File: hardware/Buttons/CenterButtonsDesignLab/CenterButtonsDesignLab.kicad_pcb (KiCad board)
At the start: 2 copper layers, 28 x 99 mm, 6 parts, among them J1 Conn_01x01, J2 Conn_01x01, J3 Conn_01x03, SW1 SW_Push, SW2 SW_Push, SW3 SW_Push

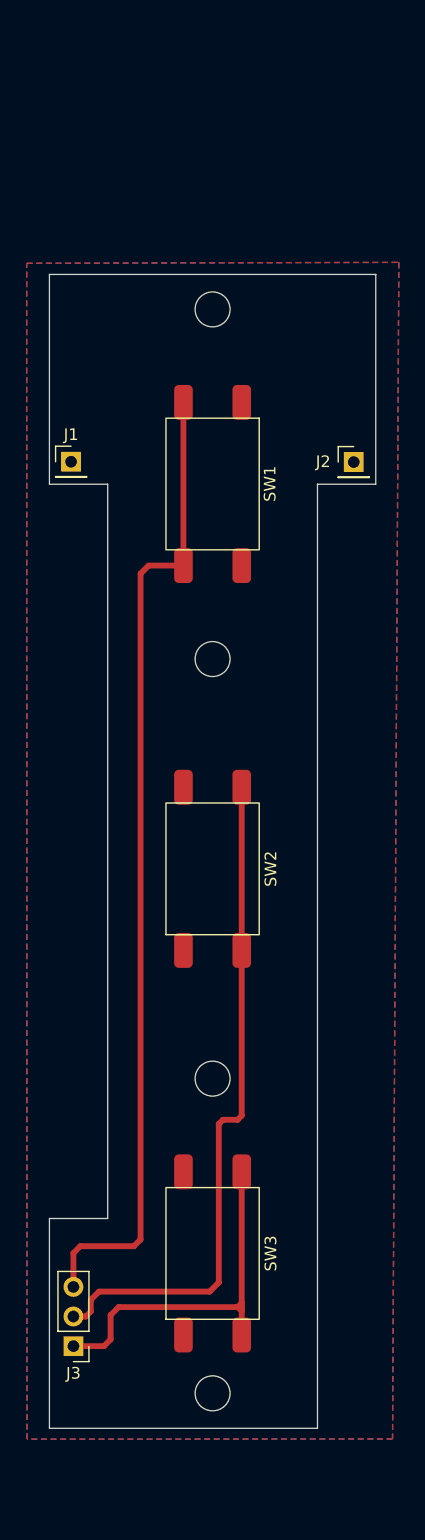
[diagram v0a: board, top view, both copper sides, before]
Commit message: Changes of button started
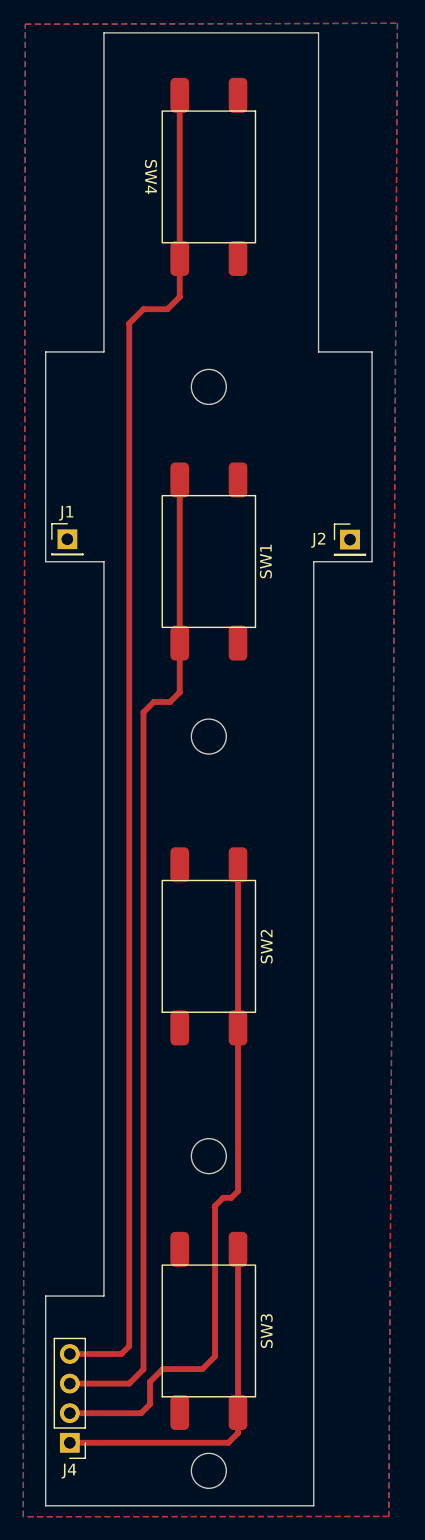
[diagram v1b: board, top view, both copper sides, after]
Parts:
- removed J3: Conn_01x03, Connector_PinHeader_2.54mm:PinHeader_1x03_P2.54mm_Vertical
- added J4: Conn_01x04, Connector_PinHeader_2.54mm:PinHeader_1x04_P2.54mm_Vertical, F.Cu at (166.9, 140.3)
- added SW4: SW_Push, Design:Button, F.Cu at (178.8, 31.7)
- moved J1 6.66 mm to (166.7, 62.7)
- moved SW3 6.66 mm to (178.8, 130.7)
- moved J2 6.66 mm to (190.9, 62.8)
- moved SW1 6.66 mm to (178.8, 64.7)
- moved SW2 6.66 mm to (178.8, 97.7)
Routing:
- net /D9: track 0.00 -> 115.7 mm
- net /D7: track 32.2 -> 30.5 mm
- net /D1: track 84.2 -> 85.2 mm
- net /D4: track 58.3 -> 59.0 mm
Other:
- board size 28 x 99 mm -> 28 x 126.4 mm

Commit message: New changes in the center buttons
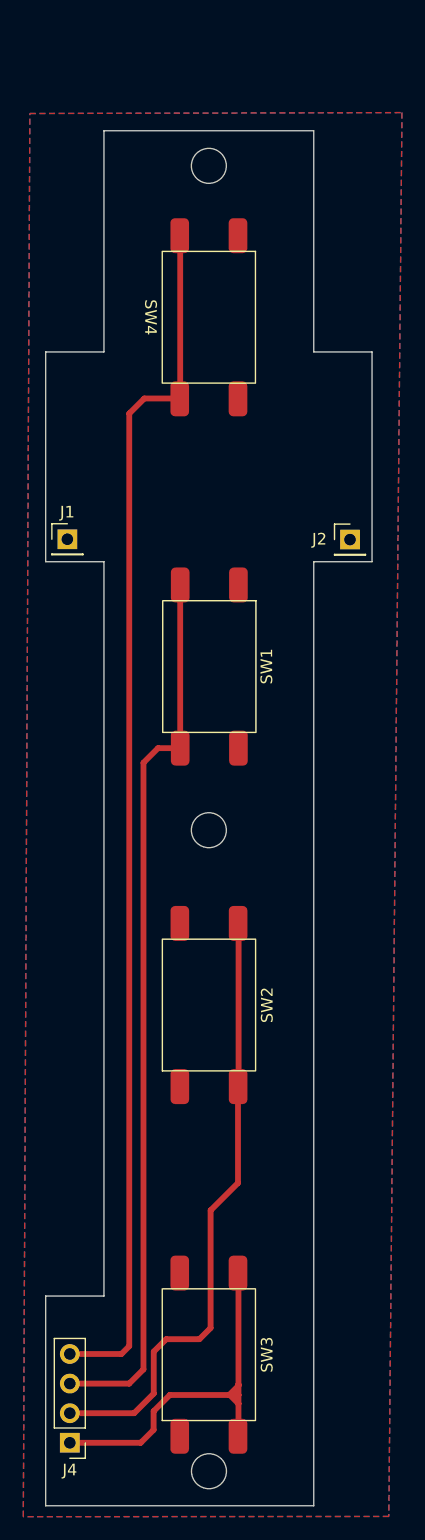
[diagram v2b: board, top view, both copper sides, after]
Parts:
- moved SW4 12.0 mm to (178.8, 43.7)
- moved SW1 9.01 mm to (178.9, 73.7)
- moved SW2 5.03 mm to (178.8, 102.7)
- moved SW3 2.04 mm to (178.8, 132.7)
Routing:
- net /D9: track 115.7 -> 104.3 mm
- net /D1: track 85.2 -> 76.5 mm
- net /D4: track 59.0 -> 53.0 mm
- net /D7: track 30.5 -> 33.5 mm
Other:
- board size 28 x 126.4 mm -> 28 x 118 mm

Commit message: Update all PCB and schematics
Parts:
- removed J2: Conn_01x01, Connector_PinHeader_2.54mm:PinHeader_1x01_P2.54mm_Vertical
- removed J4: Conn_01x04, Connector_PinHeader_2.54mm:PinHeader_1x04_P2.54mm_Vertical
- J1: value Conn_01x01 -> Conn_01x05; footprint Connector_PinHeader_2.54mm:PinHeader_1x01_P2.54mm_Vertical -> Design:JST_S5B-PH-K-S_LF__SN_; moved to B.Cu
- moved J1 76.8 mm to (171.1, 139.4), turned to 90 degrees
- moved SW3 4.99 mm to (178.8, 127.7)
- moved SW2 3.00 mm to (178.8, 99.7)
- moved SW1 1.96 mm to (178.8, 71.7)
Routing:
- net /D7: track 33.5 -> 30.9 mm
- net /D4: track 53.0 -> 54.7 mm
- net /D9: track 104.3 -> 102.7 mm
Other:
- board size 28 x 118 mm -> 23 x 118 mm
- board text removed: "GND"
